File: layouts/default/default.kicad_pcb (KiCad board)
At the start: 2 copper layers, 44 parts

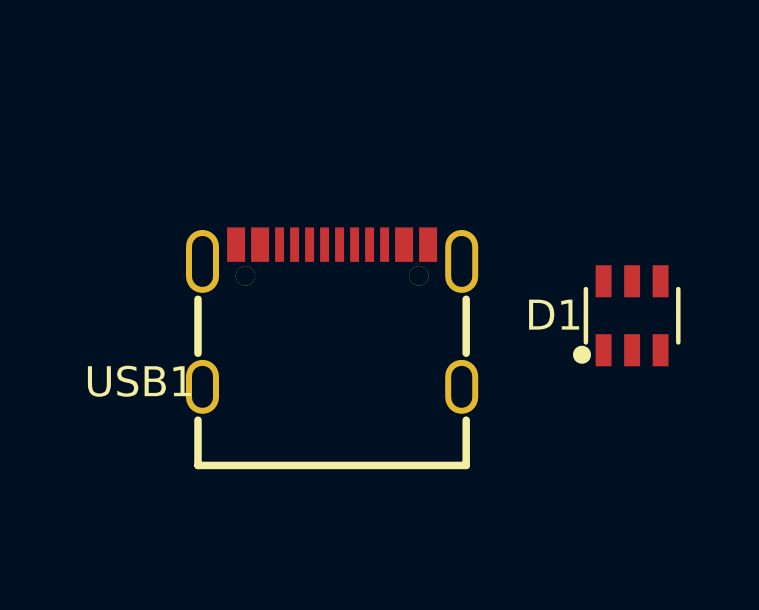
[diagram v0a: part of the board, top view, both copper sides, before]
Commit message: Add local BMP581 footprint
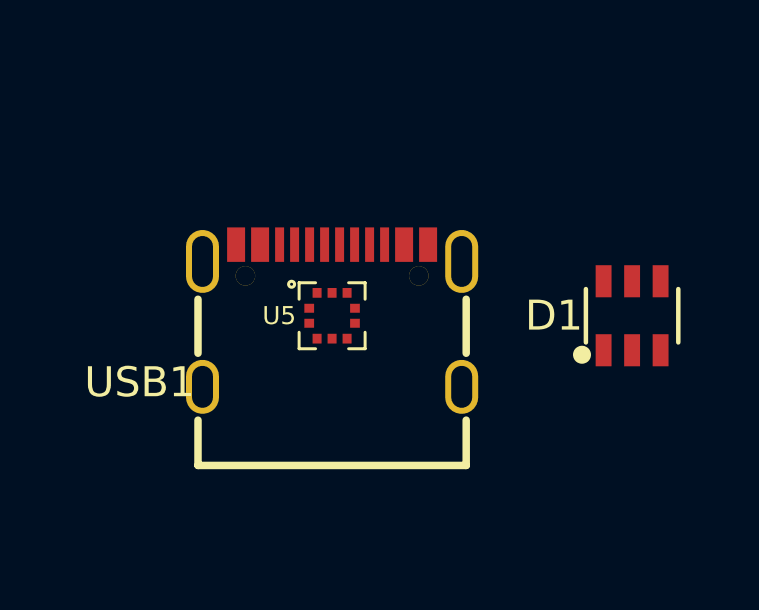
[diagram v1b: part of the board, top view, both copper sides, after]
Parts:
- added U5: , Bosch_Sensortec_BMP581:BMP581_LGA10_2x2mm, F.Cu at (0.00, 0.00)

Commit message: Doc, gerber, kicad
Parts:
- added BZ1: , Same_Sky_CSS_J4D20_SMT_TR:CSS-J4D20-SMT-TR, F.Cu at (9.00, 13.5)
- added J1: , JST_S2B_PH_SM4_TB:S2B-PH-SM4-TB, F.Cu at (0.00, -5.25)
- added J2: , Local_DebugPads:DebugPads_1x06_1.27mm, F.Cu at (9.75, -4.50)
- added Q1: , Alpha_Omega_AO3400A:AO3400A, F.Cu at (13.5, 3.50)
- added Q2: , Alpha_Omega_AO3400A:AO3400A, F.Cu at (21.0, -3.00)
- added SW1: , CK_KMR211NG_LFS:KMR211NG_LFS, F.Cu at (16.2, 10.5)
- moved C5 95.5 mm to (12.8, 17.8)
- moved C10 82.5 mm to (34.0, -21.5)
- moved C11 82.5 mm to (34.0, -41.5)
- moved C12 82.5 mm to (34.0, -31.5)
- moved C13 82.5 mm to (34.0, -51.5)
- moved C14 82.5 mm to (34.0, -61.5)
- moved C3 82.5 mm to (34.0, 48.5)
- moved C4 82.5 mm to (34.0, 38.5)
- moved C6 82.5 mm to (34.0, 28.5)
- moved C7 82.5 mm to (34.0, 8.50)
- moved C8 82.5 mm to (34.0, -1.50)
- moved C9 82.5 mm to (34.0, -11.5)
- moved R1 82.5 mm to (34.0, -71.5)
- moved R10 80.0 mm to (160.0, -230.0)
- moved R11 80.0 mm to (160.0, -240.0)
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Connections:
- U4 pad 11: INT -> 11
- U4 pad 8: INT-1 -> INT
- U5 pad 7: INT-1 -> INT
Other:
- board outline added: 90 x 45 mm

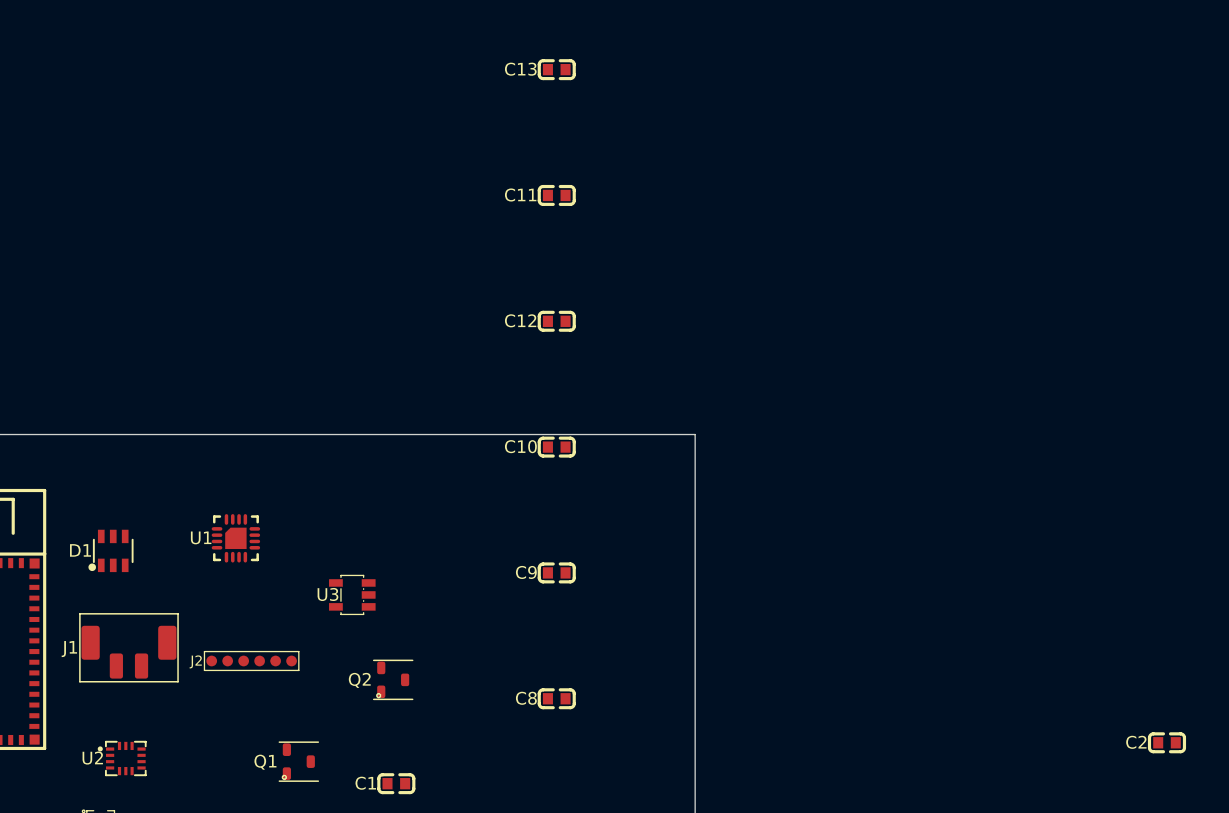
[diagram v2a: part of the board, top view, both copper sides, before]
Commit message: Add hard-off power path and bootloader buttons
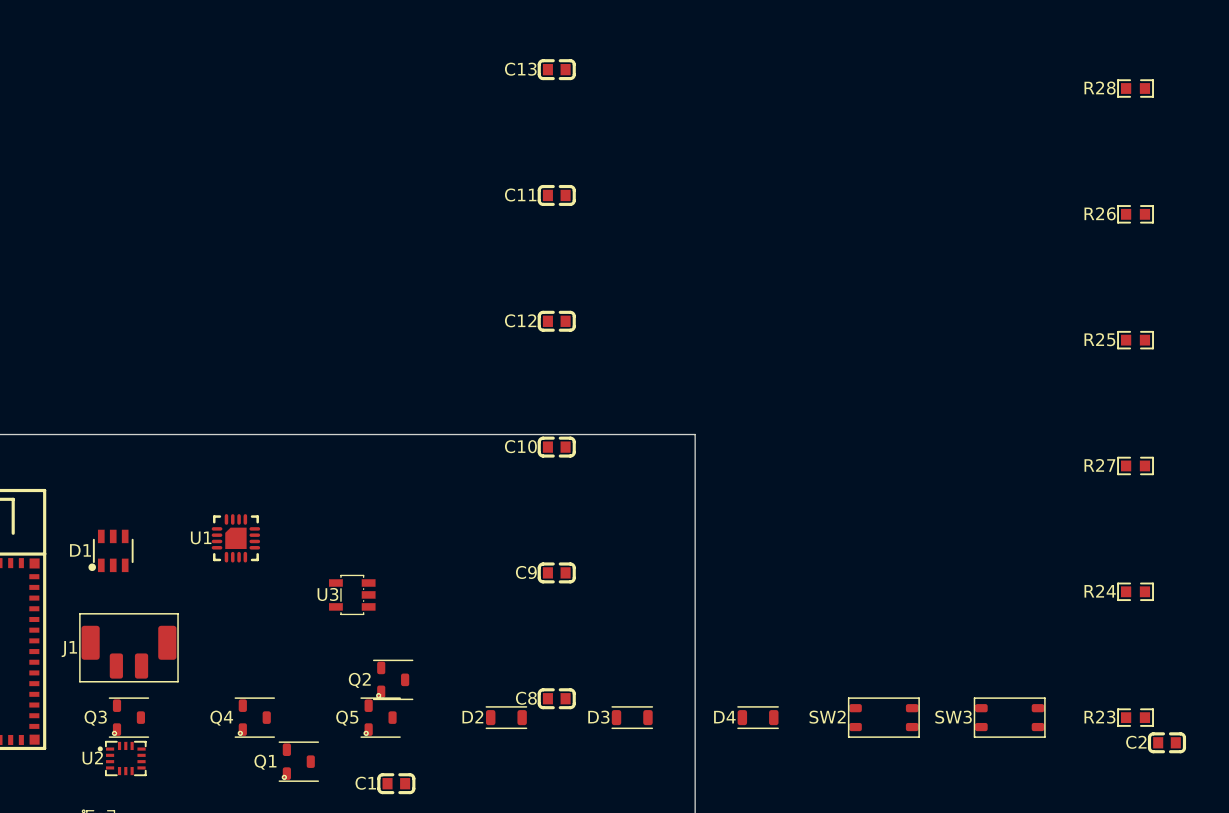
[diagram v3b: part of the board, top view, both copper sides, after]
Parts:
- removed J2: , Local_DebugPads:DebugPads_1x06_1.27mm
- added D2: , Diodes_Inc_1N4148W:1N4148W, F.Cu at (30.0, 0.00)
- added D3: , Diodes_Inc_1N4148W:1N4148W, F.Cu at (40.0, 0.00)
- added D4: , Diodes_Inc_1N4148W:1N4148W, F.Cu at (50.0, 0.00)
- added Q3: , Alpha_Omega_AO3400A:AO3400A, F.Cu at (0.00, 0.00)
- added Q4: , Diodes_Inc_DMP3098L:DMP3098L, F.Cu at (10.0, 0.00)
- added Q5: , Alpha_Omega_AO3400A:AO3400A, F.Cu at (20.0, 0.00)
- added R23: 1MΩ ±1%, UNI_ROYAL_0603WAF1004T5E:R0603, F.Cu at (80.0, 0.00)
- added R24: 4.7kΩ ±1%, UNI_ROYAL_0603WAF4701T5E:R0603, F.Cu at (80.0, -10.0)
- added R25: 1MΩ ±1%, UNI_ROYAL_0603WAF1004T5E:R0603, F.Cu at (80.0, -30.0)
- added R26: 100kΩ ±1%, UNI_ROYAL_0603WAF1003T5E:R0603, F.Cu at (80.0, -40.0)
- added R27: 100Ω ±1%, UNI_ROYAL_0603WAF1000T5E:R0603, F.Cu at (80.0, -20.0)
- added R28: 1MΩ ±1%, UNI_ROYAL_0603WAF1004T5E:R0603, F.Cu at (80.0, -50.0)
- added SW2: , CK_KMR211NG_LFS:KMR211NG_LFS, F.Cu at (60.0, 0.00)
- added SW3: , CK_KMR211NG_LFS:KMR211NG_LFS, F.Cu at (70.0, 0.00)
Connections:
- J1 pad 1: hv -> bat_raw-hv
- SW1 pad 1: BOOT_USER_BTN_N -> PWR_SW_N
- SW1 pad 2: BOOT_USER_BTN_N -> PWR_SW_N
- U1 pad 15: GND -> CHG_SYSOFF
- U4 pad 11: 11 -> PWR_BTN_N
- U4 pad 39: TXD0 -> 39
- U4 pad 40: RXD0 -> 40

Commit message: Boot, reset, USB protection
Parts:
- SW2: footprint CK_KMR211NG_LFS:KMR211NG_LFS -> CK_KMR211NG_LFS:KMR211NG_LFS_BOOT
- SW3: footprint CK_KMR211NG_LFS:KMR211NG_LFS -> CK_KMR211NG_LFS:KMR211NG_LFS_RST
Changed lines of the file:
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@@
 			)
 		)
-		(property "LCSC" "C7519"
+		(property "LCSC" "C2969755"
 			(at 0 0 0)
 			(layer "User.9")
@@
 			(hide yes)
 		)
-		(property "Partnumber" "USBLC6-2SC6"
+		(property "Partnumber" "USBLC6-2SC6Y"
 			(at 0 0 0)
 			(layer "User.9")
 			(hide yes)
 		)
-		(property "Datasheet" "https://www.lcsc.com/datasheet/lcsc_datasheet_2410121836_STMicroelectronics-USBLC6-2SC6_C7519.pdf"
+		(property "Datasheet" "https://www.st.com/resource/en/datasheet/usblc6-2sc6.pdf"
 			(at 0 0 0)
 			(layer "User.9")
@@
 			(hide yes)
 		)
-		(property "lcsc_id" "C7519"
+		(property "lcsc_id" "C2969755"
 			(at 0 0 0)
 			(layer "User.9")
@@
 		)
 	)
-	(footprint "CK_KMR211NG_LFS:KMR211NG_LFS"
+	(footprint "CK_KMR211NG_LFS:KMR211NG_LFS_BOOT"
 		(layer "F.Cu")
 		(at 60 0 0)
@@
 			(layer "F.CrtYd")
 		)
+		(fp_text user "BOOT"
+			(at 0 -2.65 0)
+			(layer "F.SilkS")
+			(effects
+				(font
+					(size 0.8 0.8)
+					(thickness 0.1)
+				)
+			)
+		)
 		(pad "1" smd roundrect
 			(at -2.25 0.75 0)
@@
 		)
 	)
-	(footprint "CK_KMR211NG_LFS:KMR211NG_LFS"
+	(footprint "CK_KMR211NG_LFS:KMR211NG_LFS_RST"
 		(layer "F.Cu")
 		(at 70 0 0)
@@
 			(layer "F.CrtYd")
 		)
+		(fp_text user "RST"
+			(at 0 -2.65 0)
+			(layer "F.SilkS")
+			(effects
+				(font
+					(size 0.8 0.8)
+					(thickness 0.1)
+				)
+			)
+		)
 		(pad "1" smd roundrect
